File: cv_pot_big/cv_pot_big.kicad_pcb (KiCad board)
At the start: 2 copper layers, 24.2 x 18 mm, 13 parts, among them J1 I/O connector, U1 HT7550-1, U2 TLV6001UIDBVR

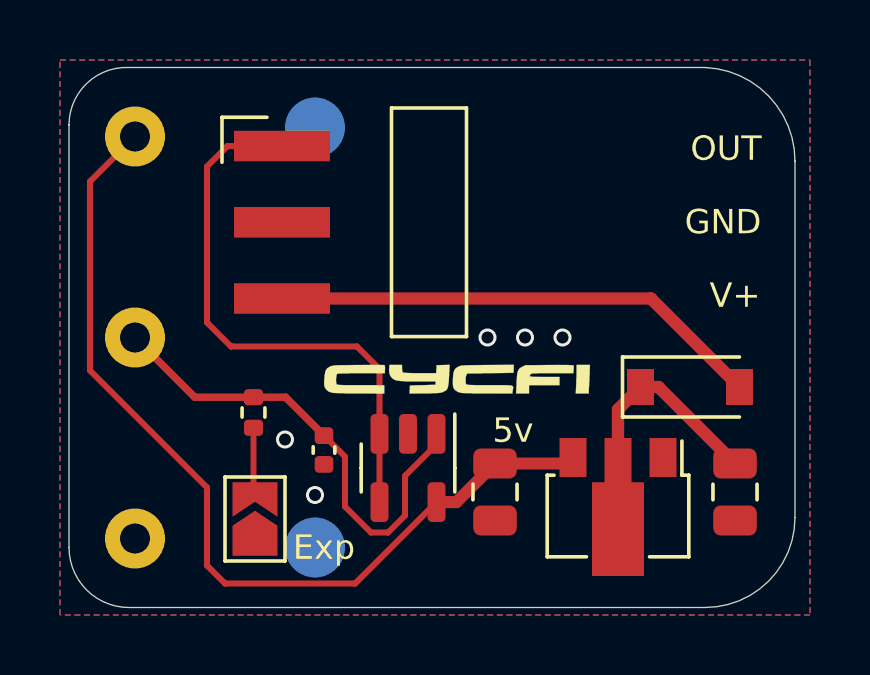
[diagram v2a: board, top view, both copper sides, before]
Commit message: Added 1k output resistor
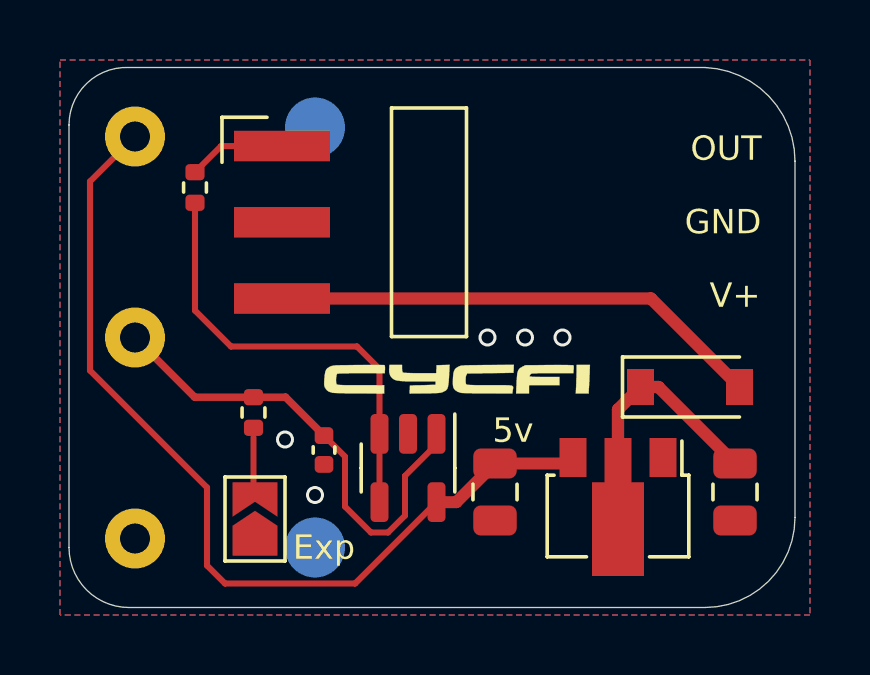
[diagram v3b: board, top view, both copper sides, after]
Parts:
- added R2: 1k, Resistor_SMD:R_0402_1005Metric, F.Cu at (138.0, 75.0)
- R1: value 4.7k -> 100k
- RV1: value 25k -> 500k
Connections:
- U2 pad 3: OUT -> Net-(U2-Pad3)
- U2 pad 4: OUT -> Net-(U2-Pad3)
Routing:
- net OUT: track 18.8 -> 3.26 mm
- net Net-(U2-Pad3): track 0.00 -> 15.0 mm
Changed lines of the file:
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@@
   (net 6 "OUT")
   (net 7 "Net-(JP1-Pad2)")
+  (net 8 "Net-(U2-Pad3)")
   (footprint "cycfi_library:bourns_pdb241" (layer "F.Cu")
     (at 136 80)
-    (property "Sheetfile" "cv_pot_big.kicad_sch")
+    (property "Sheetfile" "File: cv_pot_big.kicad_sch")
     (property "Sheetname" "")
     (attr smd)
@@
       (effects (font (size 1 1) (thickness 0.15)))
     )
-    (fp_text value "25k" (at 0 11.3 unlocked) (layer "F.Fab")
+    (fp_text value "500k" (at 0 11.3 unlocked) (layer "F.Fab")
       (effects (font (size 1 1) (thickness 0.15)))
     )
@@
   (footprint "cycfi_library:pin_header_1x3p_2.54mm_smd_horizontal" (layer "F.Cu")
     (at 140.9 73.62)
-    (property "Sheetfile" "cv_pot_big.kicad_sch")
+    (property "Sheetfile" "File: cv_pot_big.kicad_sch")
     (property "Sheetname" "")
     (attr through_hole)
@@
     (descr "SOT, 5 Pin (https://www.jedec.org/sites/default/files/docs/Mo-178c.PDF variant AA), generated with kicad-footprint-generator ipc_gullwing_generator.py")
     (tags "SOT TO_SOT_SMD")
-    (property "Sheetfile" "cv_pot_big.kicad_sch")
+    (property "Sheetfile" "File: cv_pot_big.kicad_sch")
     (property "Sheetname" "")
     (attr smd)
@@
       (net 2 "GND") (pinfunction "V-") (pintype "power_in"))
     (pad "3" smd roundrect (at -1.1375 0.95 270) (size 1.325 0.6) (layers "F.Cu" "F.Paste" "F.Mask") (roundrect_rratio 0.25)
-      (net 6 "OUT") (pinfunction "-") (pintype "input"))
+      (net 8 "Net-(U2-Pad3)") (pinfunction "-") (pintype "input"))
     (pad "4" smd roundrect (at 1.1375 0.95 270) (size 1.325 0.6) (layers "F.Cu" "F.Paste" "F.Mask") (roundrect_rratio 0.25)
-      (net 6 "OUT") (pintype "output"))
+      (net 8 "Net-(U2-Pad3)") (pintype "output"))
     (pad "5" smd roundrect (at 1.1375 -0.95 270) (size 1.325 0.6) (layers "F.Cu" "F.Paste" "F.Mask") (roundrect_rratio 0.25)
       (net 3 "5v") (pinfunction "V+") (pintype "power_in"))
@@
     (tags "capacitor")
     (property "LCSC" "C15850")
-    (property "Sheetfile" "cv_pot_big.kicad_sch")
+    (property "Sheetfile" "File: cv_pot_big.kicad_sch")
     (property "Sheetname" "")
     (attr smd)
@@
     (tags "SOD-123")
     (property "LCSC" "C81598")
-    (property "Sheetfile" "cv_pot_big.kicad_sch")
+    (property "Sheetfile" "File: cv_pot_big.kicad_sch")
     (property "Sheetname" "")
     (attr smd)
@@
     )
   )
-  (footprint "cycfi_library:cycfi-logo-9mm" locked (layer "F.Cu")
+  (footprint "cycfi_library:cycfi-logo-9mm" (layer "F.Cu")
     (at 146.7 81.4)
-    (attr through_hole)
+    (attr through_hole board_only)
     (fp_text reference "G***" (at 0 0) (layer "F.SilkS") hide
       (effects (font (size 1.524 1.524) (thickness 0.3)))
@@
     (tags "SOT-89-3")
     (property "LCSC" "C16106")
-    (property "Sheetfile" "cv_pot_big.kicad_sch")
+    (property "Sheetfile" "File: cv_pot_big.kicad_sch")
     (property "Sheetname" "")
     (attr smd)
@@
     (descr "Resistor SMD 0402 (1005 Metric), square (rectangular) end terminal, IPC_7351 nominal, (Body size source: IPC-SM-782 page 72, https://www.pcb-3d.com/wordpress/wp-content/uploads/ipc-sm-782a_amendment_1_and_2.pdf), generated with kicad-footprint-generator")
     (tags "resistor")
-    (property "LCSC" "C25900")
-    (property "Sheetfile" "cv_pot_big.kicad_sch")
+    (property "LCSC" "C25741")
+    (property "Sheetfile" "File: cv_pot_big.kicad_sch")
     (property "Sheetname" "")
     (attr smd)
@@
       (effects (font (size 1 1) (thickness 0.15)))
     )
-    (fp_text value "4.7k" (at 0 1.17 -90) (layer "F.Fab")
+    (fp_text value "100k" (at 0 1.17 -90) (layer "F.Fab")
       (effects (font (size 1 1) (thickness 0.15)))
     )
@@
     (tags "capacitor")
     (property "LCSC" "C15850")
-    (property "Sheetfile" "cv_pot_big.kicad_sch")
+    (property "Sheetfile" "File: cv_pot_big.kicad_sch")
     (property "Sheetname" "")
     (attr smd)
@@
     (tags "capacitor")
     (property "LCSC" "C307331")
-    (property "Sheetfile" "cv_pot_big.kicad_sch")
+    (property "Sheetfile" "File: cv_pot_big.kicad_sch")
     (property "Sheetname" "")
     (attr smd)
@@
     (descr "SMD Solder Jumper, 1x1.5mm Triangular Pads, 0.3mm gap, open")
     (tags "solder jumper open")
-    (property "Sheetfile" "cv_pot_big.kicad_sch")
+    (property "Sheetfile" "File: cv_pot_big.kicad_sch")
     (property "Sheetname" "")
     (attr exclude_from_pos_files)
@@
       ))
   )
+  (footprint "Resistor_SMD:R_0402_1005Metric" (layer "F.Cu")
+    (at 138 75 90)
+    (descr "Resistor SMD 0402 (1005 Metric), square (rectangular) end terminal, IPC_7351 nominal, (Body size source: IPC-SM-782 page 72, https://www.pcb-3d.com/wordpress/wp-content/uploads/ipc-sm-782a_amendment_1_and_2.pdf), generated with kicad-footprint-generator")
+    (tags "resistor")
+    (property "LCSC" "C11702")
+    (property "Sheetfile" "File: cv_pot_big.kicad_sch")
+    (property "Sheetname" "")
+    (attr smd)
+    (fp_text reference "R2" (at 0 -1.17 90) (layer "F.SilkS") hide
+      (effects (font (size 1 1) (thickness 0.15)))
+    )
+    (fp_text value "1k" (at 0 1.17 90) (layer "F.Fab")
+      (effects (font (size 1 1) (thickness 0.15)))
+    )
+    (fp_text user "${REFERENCE}" (at 0 0 90) (layer "F.Fab")
+      (effects (font (size 0.26 0.26) (thickness 0.04)))
+    )
+    (fp_line (start -0.153641 0.38) (end 0.153641 0.38) (layer "F.SilkS") (width 0.12))
+    (fp_line (start -0.153641 -0.38) (end 0.153641 -0.38) (layer "F.SilkS") (width 0.12))
+    (fp_line (start -0.93 0.47) (end -0.93 -0.47) (layer "F.CrtYd") (width 0.05))
+    (fp_line (start 0.93 -0.47) (end 0.93 0.47) (layer "F.CrtYd") (width 0.05))
+    (fp_line (start 0.93 0.47) (end -0.93 0.47) (layer "F.CrtYd") (width 0.05))
+    (fp_line (start -0.93 -0.47) (end 0.93 -0.47) (layer "F.CrtYd") (width 0.05))
+    (fp_line (start 0.525 -0.27) (end 0.525 0.27) (layer "F.Fab") (width 0.1))
+    (fp_line (start -0.525 0.27) (end -0.525 -0.27) (layer "F.Fab") (width 0.1))
+    (fp_line (start 0.525 0.27) (end -0.525 0.27) (layer "F.Fab") (width 0.1))
+    (fp_line (start -0.525 -0.27) (end 0.525 -0.27) (layer "F.Fab") (width 0.1))
+    (pad "1" smd roundrect (at -0.51 0 90) (size 0.54 0.64) (layers "F.Cu" "F.Paste" "F.Mask") (roundrect_rratio 0.25)
+      (net 8 "Net-(U2-Pad3)") (pintype "passive"))
+    (pad "2" smd roundrect (at 0.51 0 90) (size 0.54 0.64) (layers "F.Cu" "F.Paste" "F.Mask") (roundrect_rratio 0.25)
+      (net 6 "OUT") (pintype "passive"))
+    (model "${KICAD6_3DMODEL_DIR}/Resistor_SMD.3dshapes/R_0402_1005Metric.wrl"
+      (offset (xyz 0 0 0))
+      (scale (xyz 1 1 1))
+      (rotate (xyz 0 0 0))
+    )
+  )
   (footprint "cycfi_library:single-pad-2x2-circular" (layer "B.Cu")
     (at 142 73 180)
-    (property "Sheetfile" "cv_pot_big.kicad_sch")
+    (property "Sheetfile" "File: cv_pot_big.kicad_sch")
     (property "Sheetname" "")
     (attr through_hole)
@@
   (footprint "cycfi_library:single-pad-2x2-circular" (layer "B.Cu")
     (at 142 87 180)
-    (property "Sheetfile" "cv_pot_big.kicad_sch")
+    (property "Sheetfile" "File: cv_pot_big.kicad_sch")
     (property "Sheetname" "")
     (attr through_hole)
@@
   (segment (start 153.2 78.7) (end 140.9 78.7) (width 0.4084) (layer "F.Cu") (net 5))
   (segment (start 156.15 81.65) (end 153.2 78.7) (width 0.4084) (layer "F.Cu") (net 5))
-  (segment (start 144.15 81.05) (end 143.4 80.3) (width 0.2032) (layer "F.Cu") (net 6))
-  (segment (start 138.4 74.3) (end 139.08 73.62) (width 0.2032) (layer "F.Cu") (net 6))
-  (segment (start 144.15 85.4875) (end 144.15 83.2125) (width 0.2) (layer "F.Cu") (net 6))
-  (segment (start 143.4 80.3) (end 139.2 80.3) (width 0.2032) (layer "F.Cu") (net 6))
-  (segment (start 144.15 83.2125) (end 144.15 81.05) (width 0.2032) (layer "F.Cu") (net 6))
-  (segment (start 138.4 79.5) (end 138.4 74.3) (width 0.2032) (layer "F.Cu") (net 6))
-  (segment (start 139.08 73.62) (end 140.9 73.62) (width 0.2032) (layer "F.Cu") (net 6))
-  (segment (start 139.2 80.3) (end 138.4 79.5) (width 0.2032) (layer "F.Cu") (net 6))
+  (segment (start 140.9 73.62) (end 138.87 73.62) (width 0.2032) (layer "F.Cu") (net 6))
+  (segment (start 138.87 73.62) (end 138 74.49) (width 0.2032) (layer "F.Cu") (net 6))
   (segment (start 139.95 85.275) (end 140 85.325) (width 0.2) (layer "F.Cu") (net 7))
   (segment (start 139.95 83.325) (end 139.95 85.275) (width 0.2) (layer "F.Cu") (net 7))
+  (segment (start 143.4 80.3) (end 144.15 81.05) (width 0.2032) (layer "F.Cu") (net 8))
+  (segment (start 144.15 85.4875) (end 144.15 83.2125) (width 0.2) (layer "F.Cu") (net 8))
+  (segment (start 139.2 80.3) (end 143.4 80.3) (width 0.2032) (layer "F.Cu") (net 8))
+  (segment (start 144.15 81.05) (end 144.15 83.2125) (width 0.2032) (layer "F.Cu") (net 8))
+  (segment (start 138 79.1) (end 139.2 80.3) (width 0.2032) (layer "F.Cu") (net 8))
+  (segment (start 138 75.51) (end 138 79.1) (width 0.2032) (layer "F.Cu") (net 8))
   (zone (net 2) (net_name "GND") (layer "F.Cu") (hatch edge 0.508)
     (connect_pads (clearance 0.3))

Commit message: Big pot update: the header now points towards the terminals side
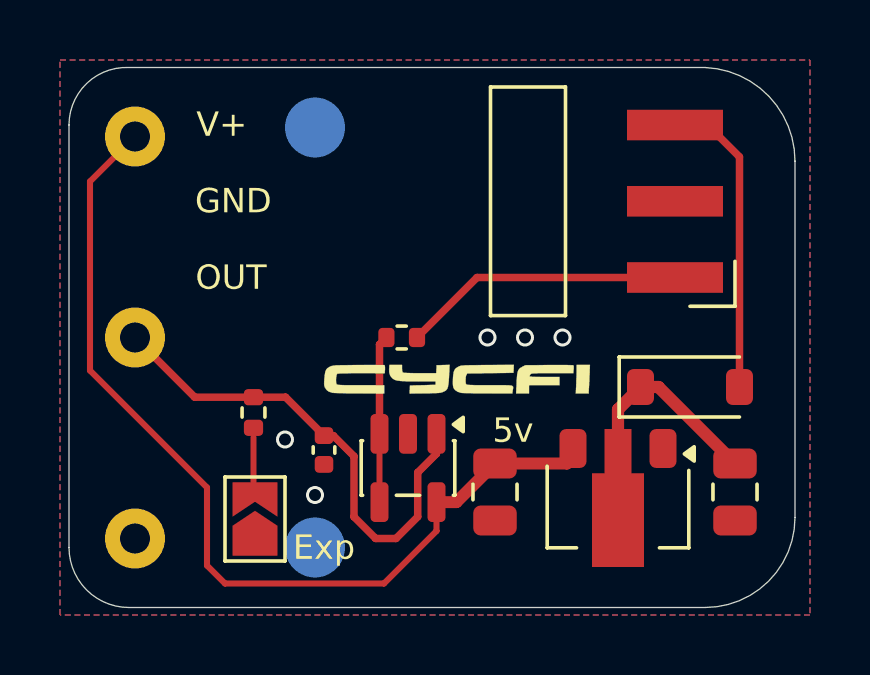
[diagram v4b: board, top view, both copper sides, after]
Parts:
- moved J1 13.2 mm to (154.0, 75.5), turned to 180 degrees
- moved R2 8.51 mm to (144.9, 80.0), turned to 0 degrees
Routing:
- net Net-(U2--): track 15.0 -> 5.58 mm
- net V+: track 16.5 -> 10.3 mm
- net OUT: track 3.26 -> 9.43 mm
- net /pot_center: track 16.1 -> 16.7 mm
- net 5v: track 30.7 -> 31.3 mm
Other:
- rule pad_to_mask_clearance: 0.2 -> 0

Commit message: Update with log and exp taper
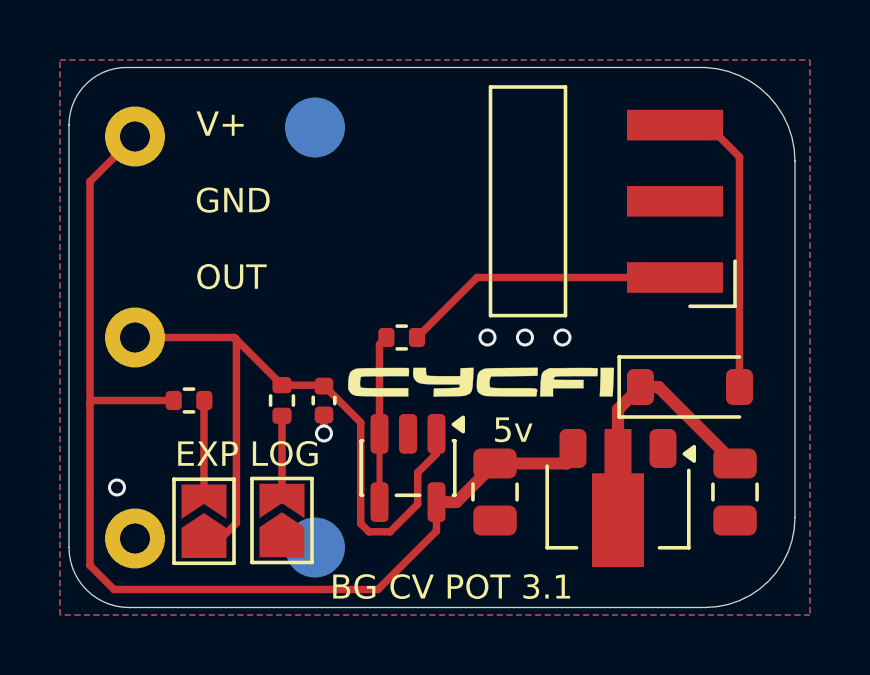
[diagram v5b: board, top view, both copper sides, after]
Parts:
- added JP2: exp shunt, Jumper:SolderJumper-2_P1.3mm_Open_TrianglePad1.0x1.5mm, F.Cu at (138.3, 86.1)
- added R3: 100k, Resistor_SMD:R_0402_1005Metric, F.Cu at (137.8, 82.1)
- JP1: value exp shunt -> log shunt
- moved C3 1.65 mm to (142.3, 82.1)
- moved R1 1.03 mm to (140.9, 82.1)
- moved JP1 0.90 mm to (140.9, 86.1)
- moved G*** 0.81 mm to (147.5, 81.5)
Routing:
- net /pot_center: track 16.7 -> 24.6 mm
- net 5v: track 31.3 -> 36.6 mm
- net Net-(JP2-B): track 0.00 -> 3.30 mm
- net Net-(JP1-B): track 2.02 -> 2.77 mm
- net GND: track 0.00 -> 0.62 mm
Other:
- board text added: "BG CV POT 3.1"
- board text added: "EXP"
- board text added: "LOG"
- board text removed: "Exp"

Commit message: Added Opamp bypass cap
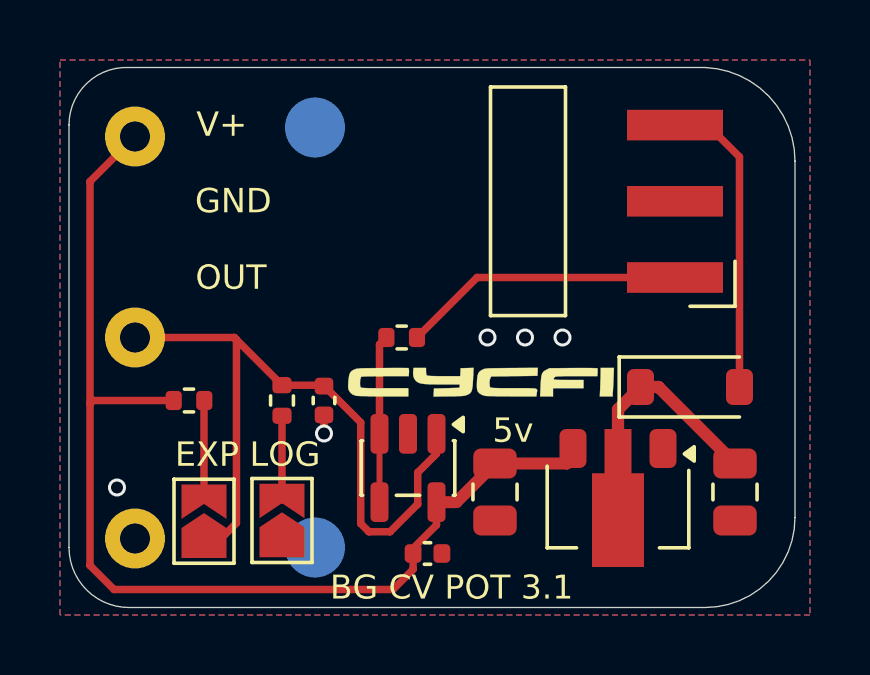
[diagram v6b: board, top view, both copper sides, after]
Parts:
- added C4: 100nF, Capacitor_SMD:C_0402_1005Metric, F.Cu at (145.8, 87.2)
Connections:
- net /pot_center renamed /pot_wiper
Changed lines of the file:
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@@
 	(net 2 "GND")
 	(net 3 "5v")
-	(net 4 "/pot_center")
+	(net 4 "/pot_wiper")
 	(net 5 "V+")
 	(net 6 "OUT")
@@
 			(layers "*.Cu" "*.Mask")
 			(remove_unused_layers no)
-			(net 4 "/pot_center")
+			(net 4 "/pot_wiper")
 			(pinfunction "2")
 			(pintype "passive")
@@
 			)
 		)
-		(property "Datasheet" ""
+		(property "Datasheet" "~"
 			(at 0 0 0)
 			(layer "F.Fab")
@@
 			)
 		)
-		(property "Description" ""
+		(property "Description" "Generic connector, single row, 01x03, script generated (kicad-library-utils/schlib/autogen/connector/)"
 			(at 0 0 0)
 			(layer "F.Fab")
@@
 			)
 		)
-		(property ki_fp_filters "Pin_Header_Straight_1X* Pin_Header_Angled_1X* Socket_Strip_Straight_1X* Socket_Strip_Angled_1X*")
+		(property ki_fp_filters "Connector*:*_1x??_*")
 		(sheetname "/")
 		(sheetfile "cv_pot_big.kicad_sch")
@@
 			(layers "F.Cu" "F.Mask" "F.Paste")
 			(net 6 "OUT")
-			(pinfunction "P1")
+			(pinfunction "Pin_1")
 			(pintype "passive")
 		)
@@
 			(layers "F.Cu" "F.Mask" "F.Paste")
 			(net 2 "GND")
-			(pinfunction "P2")
+			(pinfunction "Pin_2")
 			(pintype "passive")
 		)
@@
 			(layers "F.Cu" "F.Mask" "F.Paste")
 			(net 5 "V+")
-			(pinfunction "P3")
+			(pinfunction "Pin_3")
 			(pintype "passive")
 		)
@@
 			(size 0.3 0.3)
 			(layers "F.Cu" "F.Mask")
-			(net 4 "/pot_center")
+			(net 4 "/pot_wiper")
 			(pinfunction "A")
 			(pintype "passive")
@@
 			(layers "F.Cu" "F.Mask" "F.Paste")
 			(roundrect_rratio 0.25)
-			(net 4 "/pot_center")
+			(net 4 "/pot_wiper")
 			(pinfunction "+")
 			(pintype "input")
@@
 			(layers "F.Cu" "F.Mask" "F.Paste")
 			(roundrect_rratio 0.25)
-			(net 4 "/pot_center")
+			(net 4 "/pot_wiper")
 			(pintype "passive")
 		)
@@
 			(layers "F.Cu" "F.Mask" "F.Paste")
 			(roundrect_rratio 0.25)
-			(net 4 "/pot_center")
+			(net 4 "/pot_wiper")
 			(pintype "passive")
 		)
@@
 		(embedded_fonts no)
 	)
+	(footprint "Capacitor_SMD:C_0402_1005Metric"
+		(layer "F.Cu")
+		(at 145.75 87.2)
+		(descr "Capacitor SMD 0402 (1005 Metric), square (rectangular) end terminal, IPC-7351 nominal, (Body size source: IPC-SM-782 page 76, https://www.pcb-3d.com/wordpress/wp-content/uploads/ipc-sm-782a_amendment_1_and_2.pdf), generated with kicad-footprint-generator")
+		(tags "capacitor")
+		(property "Reference" "C4"
+			(at 0 -1.16 0)
+			(layer "F.SilkS")
+			(hide yes)
+			(effects
+				(font
+					(size 1 1)
+					(thickness 0.15)
+				)
+			)
+		)
+		(property "Value" "100nF"
+			(at 0 1.16 0)
+			(layer "F.Fab")
+			(effects
+				(font
+					(size 1 1)
+					(thickness 0.15)
+				)
+			)
+		)
+		(property "Datasheet" "~"
+			(at 0 0 0)
+			(layer "F.Fab")
+			(hide yes)
+			(effects
+				(font
+					(size 1.27 1.27)
+					(thickness 0.15)
+				)
+			)
+		)
+		(property "Description" ""
+			(at 0 0 0)
+			(layer "F.Fab")
+			(hide yes)
+			(effects
+				(font
+					(size 1.27 1.27)
+					(thickness 0.15)
+				)
+			)
+		)
+		(property "LCSC" "C307331"
+			(at 0 0 0)
+			(unlocked yes)
+			(layer "F.Fab")
+			(hide yes)
+			(effects
+				(font
+					(size 1 1)
+					(thickness 0.15)
+				)
+			)
+		)
+		(property ki_fp_filters "C_*")
+		(sheetname "/")
+		(sheetfile "cv_pot_big.kicad_sch")
+		(attr smd)
+		(fp_line
+			(start -0.107836 -0.36)
+			(end 0.107836 -0.36)
+			(stroke
+				(width 0.12)
+				(type solid)
+			)
+			(layer "F.SilkS")
+		)
+		(fp_line
+			(start -0.107836 0.36)
+			(end 0.107836 0.36)
+			(stroke
+				(width 0.12)
+				(type solid)
+			)
+			(layer "F.SilkS")
+		)
+		(fp_rect
+			(start -0.91 -0.46)
+			(end 0.91 0.46)
+			(stroke
+				(width 0.05)
+				(type solid)
+			)
+			(fill no)
+			(layer "F.CrtYd")
+		)
+		(fp_rect
+			(start -0.5 -0.25)
+			(end 0.5 0.25)
+			(stroke
+				(width 0.1)
+				(type solid)
+			)
+			(fill no)
+			(layer "F.Fab")
+		)
+		(fp_text user "${REFERENCE}"
+			(at 0 0 0)
+			(layer "F.Fab")
+			(effects
+				(font
+					(size 0.25 0.25)
+					(thickness 0.04)
+				)
+			)
+		)
+		(pad "1" smd roundrect
+			(at -0.48 0)
+			(size 0.56 0.62)
+			(layers "F.Cu" "F.Mask" "F.Paste")
+			(roundrect_rratio 0.25)
+			(net 3 "5v")
+			(pintype "passive")
+		)
+		(pad "2" smd roundrect
+			(at 0.48 0)
+			(size 0.56 0.62)
+			(layers "F.Cu" "F.Mask" "F.Paste")
+			(roundrect_rratio 0.25)
+			(net 2 "GND")
+			(pintype "passive")
+		)
+		(embedded_fonts no)
+		(model "${KICAD9_3DMODEL_DIR}/Capacitor_SMD.3dshapes/C_0402_1005Metric.step"
+			(offset
+				(xyz 0 0 0)
+			)
+			(scale
+				(xyz 1 1 1)
+			)
+			(rotate
+				(xyz 0 0 0)
+			)
+		)
+	)
 	(footprint "Resistor_SMD:R_0402_1005Metric"
 		(layer "F.Cu")
@@
 	)
 	(segment
+		(start 135.3 88.4)
+		(end 144.6 88.4)
+		(width 0.25)
+		(layer "F.Cu")
+		(net 3)
+	)
+	(segment
 		(start 148 84.2)
 		(end 150.4 84.2)
@@
 	)
 	(segment
+		(start 134.5 82.2)
+		(end 134.5 87.6)
+		(width 0.25)
+		(layer "F.Cu")
+		(net 3)
+	)
+	(segment
 		(start 146.05 85.4875)
 		(end 146.7125 85.4875)
@@
 	)
 	(segment
-		(start 134.5 82.2)
-		(end 134.5 87.6)
+		(start 144.6 88.4)
+		(end 145.27 87.73)
+		(width 0.25)
+		(layer "F.Cu")
+		(net 3)
+	)
+	(segment
+		(start 146.05 86.25)
+		(end 146.05 85.4875)
+		(width 0.25)
+		(layer "F.Cu")
+		(net 3)
+	)
+	(segment
+		(start 145.27 87.2)
+		(end 145.27 87.03)
 		(width 0.25)
 		(layer "F.Cu")
@@
 	)
 	(segment
-		(start 134.6 82.1)
-		(end 134.5 82.2)
+		(start 145.27 87.03)
+		(end 146.05 86.25)
 		(width 0.25)
 		(layer "F.Cu")
@@
 	)
 	(segment
-		(start 144.1 88.4)
-		(end 146.05 86.45)
+		(start 134.6 82.1)
+		(end 134.5 82.2)
 		(width 0.25)
 		(layer "F.Cu")
@@
 	)
 	(segment
-		(start 135.3 88.4)
-		(end 144.1 88.4)
-		(width 0.25)
-		(layer "F.Cu")
-		(net 3)
-	)
-	(segment
-		(start 146.05 86.45)
-		(end 146.05 85.4875)
+		(start 145.27 87.73)
+		(end 145.27 87.2)
 		(width 0.25)
 		(layer "F.Cu")
